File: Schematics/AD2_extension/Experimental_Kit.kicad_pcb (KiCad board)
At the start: 2 copper layers, 69.7 x 77 mm, 15 parts, among them J1 Conn_01x05, J2 AD2, J3 Conn_01x02, J4 Conn_01x02, J5 Conn_01x03, J6 CN7, J7 CN10, J8 AD2, J9 Conn_01x02

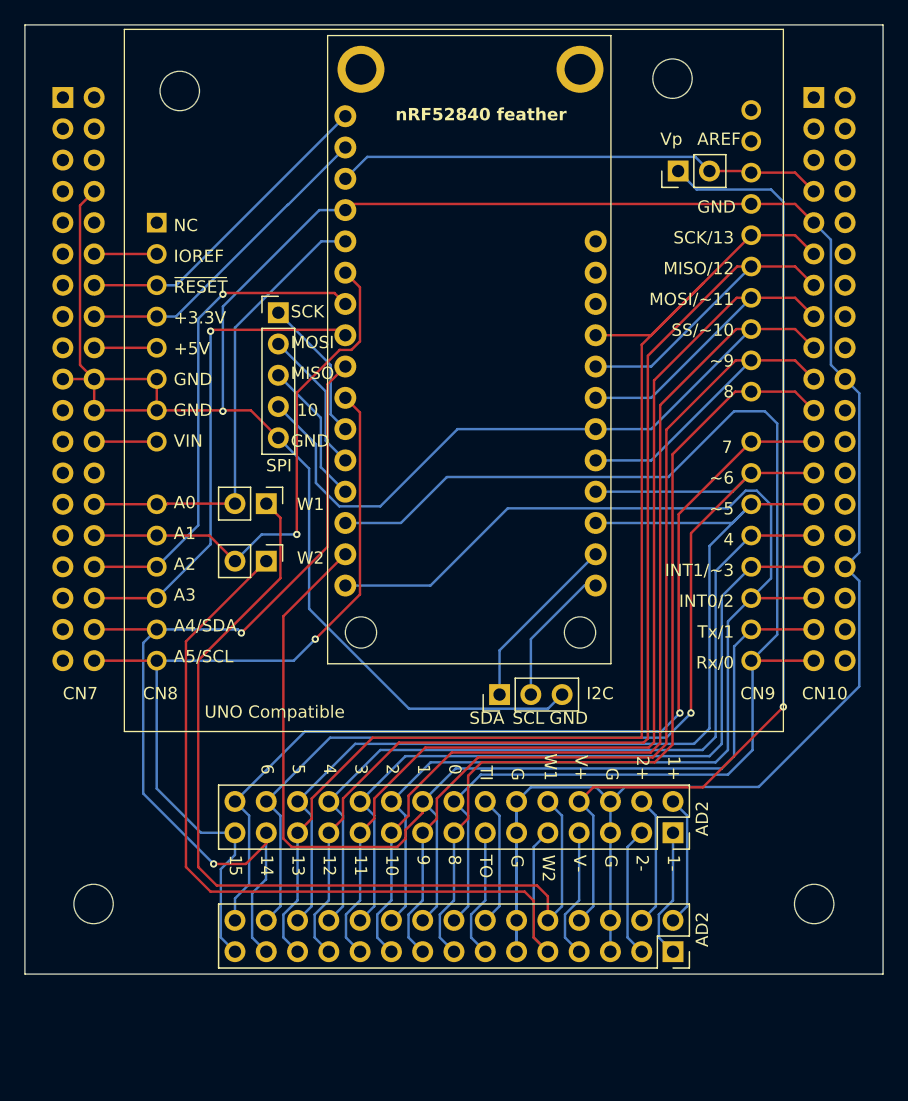
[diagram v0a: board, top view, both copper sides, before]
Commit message: AD2_extension: on-board level shifters, re-synced PCB, autorouted board
Schematic
- Replace the plug-in BSS138 module (J2/J4) with on-board circuits:
  4x 2N7002 MOSFET shifters (SDA/SCL to LCD, DIO3/DIO5 to PWM) with
  host-side pull-ups on IOREF, TXU0304 fixed-direction SPI shifter
  (VCCA=IOREF, VCCB=3V3), and an IOREF-3V3 header for Feather
- Keypad VCC moved from +3V3 to IOREF (ratiometric ADC readings)
- Add project symbol library (TXU0304PW) and sym-lib-table

PCB
- Sync footprints by UUID after re-annotation, place new parts on the
  back side between the Feather pin rows, mounting holes as H1-H4
- Net classes: Default 0.3 mm, Power 0.6 mm; bottom edge at 120.0 mm
  with copper-to-edge clearance 0.25 mm
- Autoroute with FreeRouting (optimizer threshold 0.1 %), GND pours on
  both layers; DRC: 0 errors, 0 unconnected, schematic parity clean

Co-Authored-By: Claude Fable 5.1 <noreply@anthropic.com>
(cherry picked from commit 84283bcdd4d08d66143eba964df6da12d674042d)
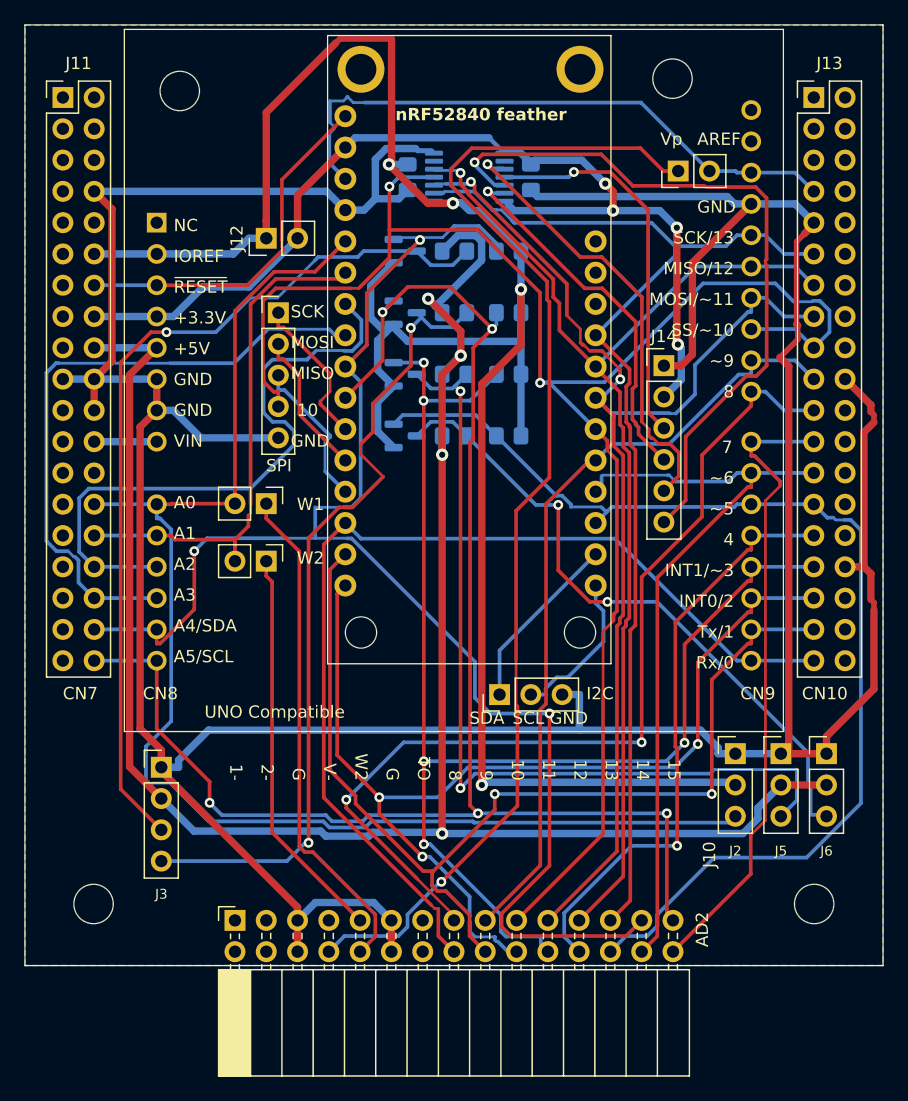
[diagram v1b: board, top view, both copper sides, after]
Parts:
- removed the J7 at (141.0, 49.5)
- removed the J8 at (129.5, 109.2)
- added C1: 100nF, Capacitor_SMD:C_0805_2012Metric_Pad1.18x1.45mm_HandSolder, B.Cu at (108.0, 56.0)
- added C2: 100nF, Capacitor_SMD:C_0805_2012Metric_Pad1.18x1.45mm_HandSolder, B.Cu at (118.0, 56.0)
- added J10: AD2, Connector_PinSocket_2.54mm:PinSocket_2x15_P2.54mm_Horizontal, F.Cu at (94.0, 116.3)
- added J11: CN7, AD2_extension:PinSocket_2x19_P2.54mm_Vertical_Mirrored, F.Cu at (80.0, 49.5)
- added J12: IOREF, Connector_PinHeader_2.54mm:PinHeader_1x02_P2.54mm_Vertical, F.Cu at (96.5, 61.0)
- added J13: CN10, AD2_extension:PinSocket_2x19_P2.54mm_Vertical_Mirrored, F.Cu at (141.0, 49.5)
- added J14: SPI, Connector_PinHeader_2.54mm:PinHeader_1x06_P2.54mm_Vertical, F.Cu at (128.8, 71.3)
- added J3: LCD, Connector_PinHeader_2.54mm:PinHeader_1x04_P2.54mm_Vertical, F.Cu at (88.0, 103.9)
- added J5: PWM, Connector_PinHeader_2.54mm:PinHeader_1x03_P2.54mm_Vertical, F.Cu at (138.3, 102.8)
- added Q1: 2N7002, Package_TO_SOT_SMD:SOT-23, B.Cu at (107.8, 62.0)
- added Q2: 2N7002, Package_TO_SOT_SMD:SOT-23, B.Cu at (107.8, 67.0)
- added Q3: 2N7002, Package_TO_SOT_SMD:SOT-23, B.Cu at (107.8, 72.0)
- added Q4: 2N7002, Package_TO_SOT_SMD:SOT-23, B.Cu at (107.8, 77.0)
- added R1: 10k, Resistor_SMD:R_0805_2012Metric_Pad1.20x1.40mm_HandSolder, B.Cu at (111.8, 62.0)
- added R2: 4.7k, Resistor_SMD:R_0805_2012Metric_Pad1.20x1.40mm_HandSolder, B.Cu at (116.2, 62.0)
- added R3: 10k, Resistor_SMD:R_0805_2012Metric_Pad1.20x1.40mm_HandSolder, B.Cu at (111.8, 67.0)
- added R4: 4.7k, Resistor_SMD:R_0805_2012Metric_Pad1.20x1.40mm_HandSolder, B.Cu at (116.2, 67.0)
- added R5: 10k, Resistor_SMD:R_0805_2012Metric_Pad1.20x1.40mm_HandSolder, B.Cu at (111.8, 72.0)
- added R6: 10k, Resistor_SMD:R_0805_2012Metric_Pad1.20x1.40mm_HandSolder, B.Cu at (116.2, 72.0)
- added R7: 10k, Resistor_SMD:R_0805_2012Metric_Pad1.20x1.40mm_HandSolder, B.Cu at (111.8, 77.0)
- added R8: 10k, Resistor_SMD:R_0805_2012Metric_Pad1.20x1.40mm_HandSolder, B.Cu at (116.2, 77.0)
- added U1: TXU0304PW, Package_SO:TSSOP-14_4.4x5mm_P0.65mm, B.Cu at (113.0, 56.0)
- A1: footprint Module:Arduino_UNO_R3 -> AD2_extension:Arduino_UNO_R3_ShieldHeaders
- J2: value AD2 -> Keypad; footprint Connector_PinSocket_2.54mm:PinSocket_2x15_P2.54mm_Vertical -> Connector_PinHeader_2.54mm:PinHeader_1x03_P2.54mm_Vertical
- J6: value CN7 -> PWM; footprint Connector_PinSocket_2.54mm:PinSocket_2x19_P2.54mm_Vertical -> Connector_PinHeader_2.54mm:PinHeader_1x03_P2.54mm_Vertical; moved to F.Cu
- J7: renamed from J3; value Conn_01x02 -> AREF
- J9: renamed from J4; value Conn_01x02 -> W1
- moved J6 81.7 mm to (142.0, 102.8), turned to 0 degrees
- moved J2 16.8 mm to (134.6, 102.8), turned to 0 degrees
- renumbered REF** to H1, REF** to H2, REF** to H3, REF** to H4, J5 to J1, J1 to J4, J9 to J8
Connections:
- J2 pad 1: /Ch1N -> GND
- J2 pad 2: /Ch1P -> /IOREF
- J2 pad 3: /Ch2N -> /A0
- J6 pad 1: unconnected-(J6-Pin_1-Pad1) -> GND
- J6 pad 2: unconnected-(J6-Pin_2-Pad2) -> +5V
- J6 pad 3: unconnected-(J6-Pin_3-Pad3) -> /DIO5_5V
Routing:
- net /IOREF: track 5.08 -> 171.9 mm, vias 0 -> 4
- net +5V: track 5.08 -> 162.4 mm, vias 0 -> 4
- net /A0: track 37.6 -> 112.3 mm
- net /LCD_SDA: track 0.00 -> 72.1 mm, vias 0 -> 1
- net /DIO3_5V: track 0.00 -> 70.1 mm, vias 0 -> 2
- net /LCD_SCL: track 0.00 -> 66.6 mm, vias 0 -> 2
- net GND: track 254.0 -> 318.0 mm, vias 1 -> 0
- net /SPI_MOSI: track 0.00 -> 59.1 mm, vias 0 -> 1
- net /SCL/A5: track 69.1 -> 127.7 mm, vias 1 -> 5
- net +3V3: track 26.1 -> 83.3 mm, vias 0 -> 4
- net /DIO5_5V: track 0.00 -> 52.9 mm, vias 0 -> 2
- net /SDA/A4: track 75.5 -> 124.0 mm, vias 2 -> 3
- net /DIO3: track 62.3 -> 106.8 mm, vias 0 -> 5
- net /W2: track 72.1 -> 32.3 mm
- net /SPI_MISO: track 0.00 -> 36.7 mm, vias 0 -> 1
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- added copper zone on B.Cu, net GND
- added copper zone on F.Cu, net GND
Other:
- board size 69.7 x 77 mm -> 69.7 x 76.4 mm
- board text added: "Dept. of EEC, HKNU 26.10.09"
- board text removed: "0"
- board text removed: "1"
- board text removed: "1+"
- board text removed: "2"
- board text removed: "2+"
- board text removed: "3"
- board text removed: "5"
- board text removed: "6"
- board text removed: "Dept. of EEC, HKNU 25.01.17"
- board text removed: "TI"
- board text removed: "V+"
